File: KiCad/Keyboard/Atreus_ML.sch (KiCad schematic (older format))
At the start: 88 parts, among them K1 CHERRY_ML, K10 CHERRY_ML, K11 CHERRY_ML, K12 CHERRY_ML, K13 CHERRY_ML, K14 CHERRY_ML, K15 CHERRY_ML, K16 CHERRY_ML, K17 CHERRY_ML, K18 CHERRY_ML, K19 CHERRY_ML, K2 CHERRY_ML, K20 CHERRY_ML, K21 CHERRY_ML, K22 CHERRY_ML, K23 CHERRY_ML, K24 CHERRY_ML, K25 CHERRY_ML, K26 CHERRY_ML, K27 CHERRY_ML, K28 CHERRY_ML, K29 CHERRY_ML, K3 CHERRY_ML, K30 CHERRY_ML, K31 CHERRY_ML, K32 CHERRY_ML, K33 CHERRY_ML, K34 CHERRY_ML, K35 CHERRY_ML, K36 CHERRY_ML, K37 CHERRY_ML, K38 CHERRY_ML, K39 CHERRY_ML, K4 CHERRY_ML, K40 CHERRY_ML, K41 CHERRY_ML, K42 CHERRY_ML, K5 CHERRY_ML, K6 CHERRY_ML, K7 CHERRY_ML, K8 CHERRY_ML, K9 CHERRY_ML, P1 CONN_01X07, P2 CONN_01X07, P3 CONN_01X07, U1 TEENSY2.0-Compact

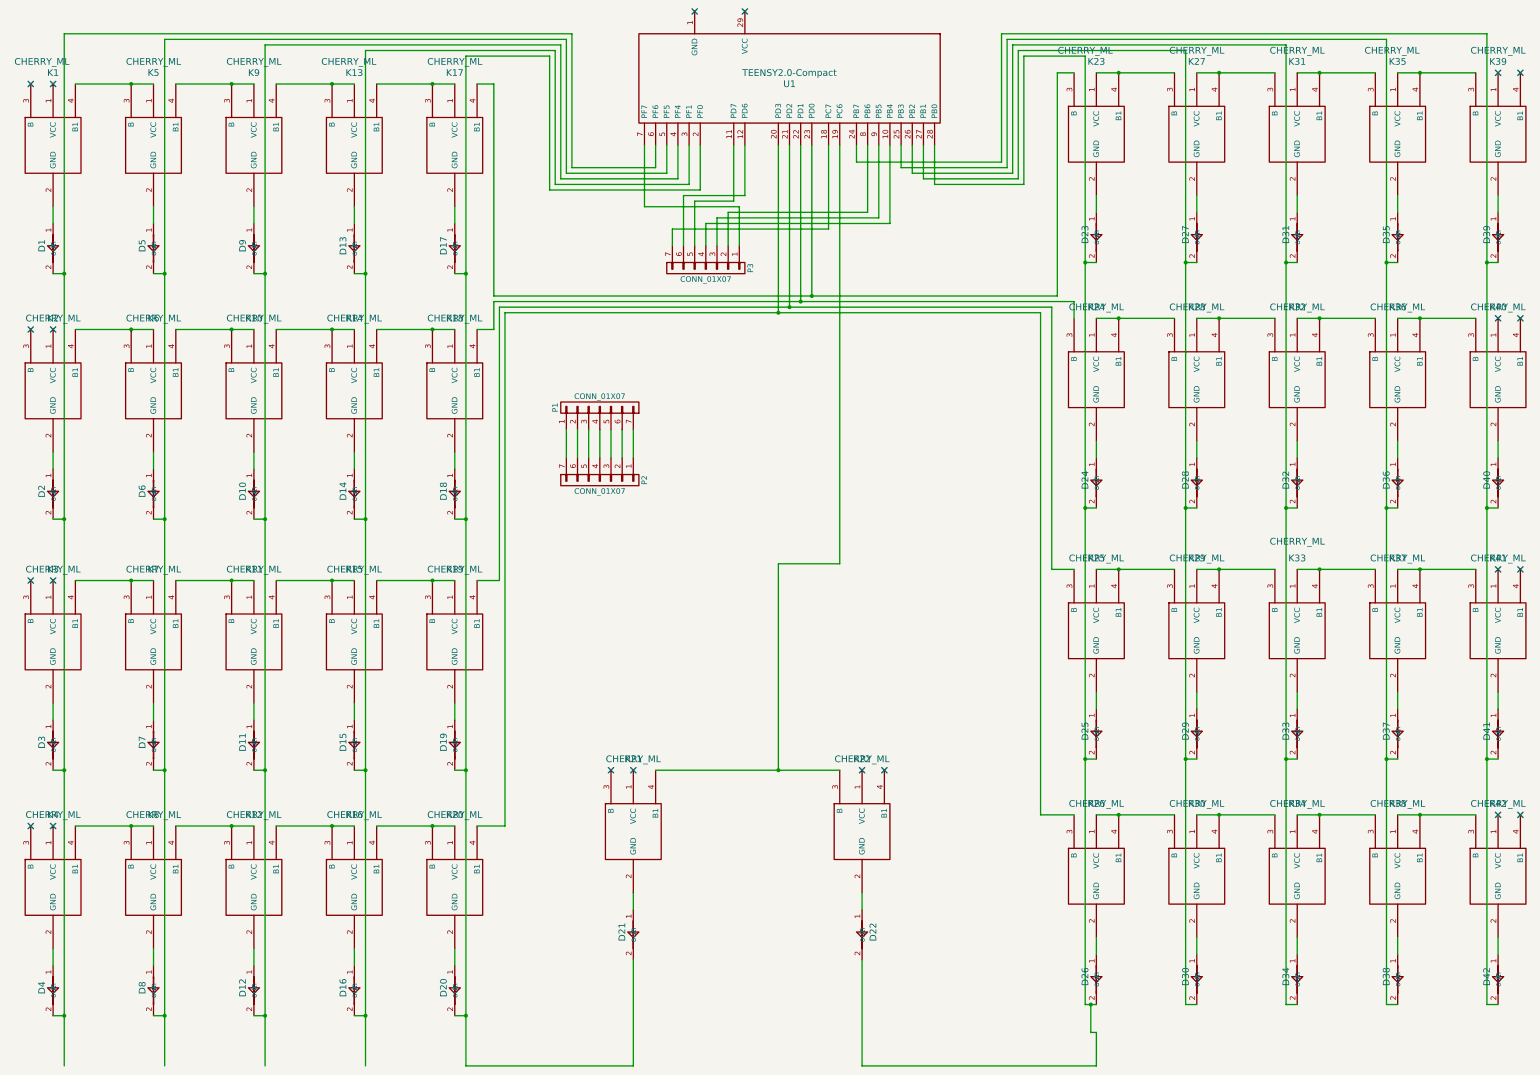
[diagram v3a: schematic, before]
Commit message: Half a fix for design and some test code
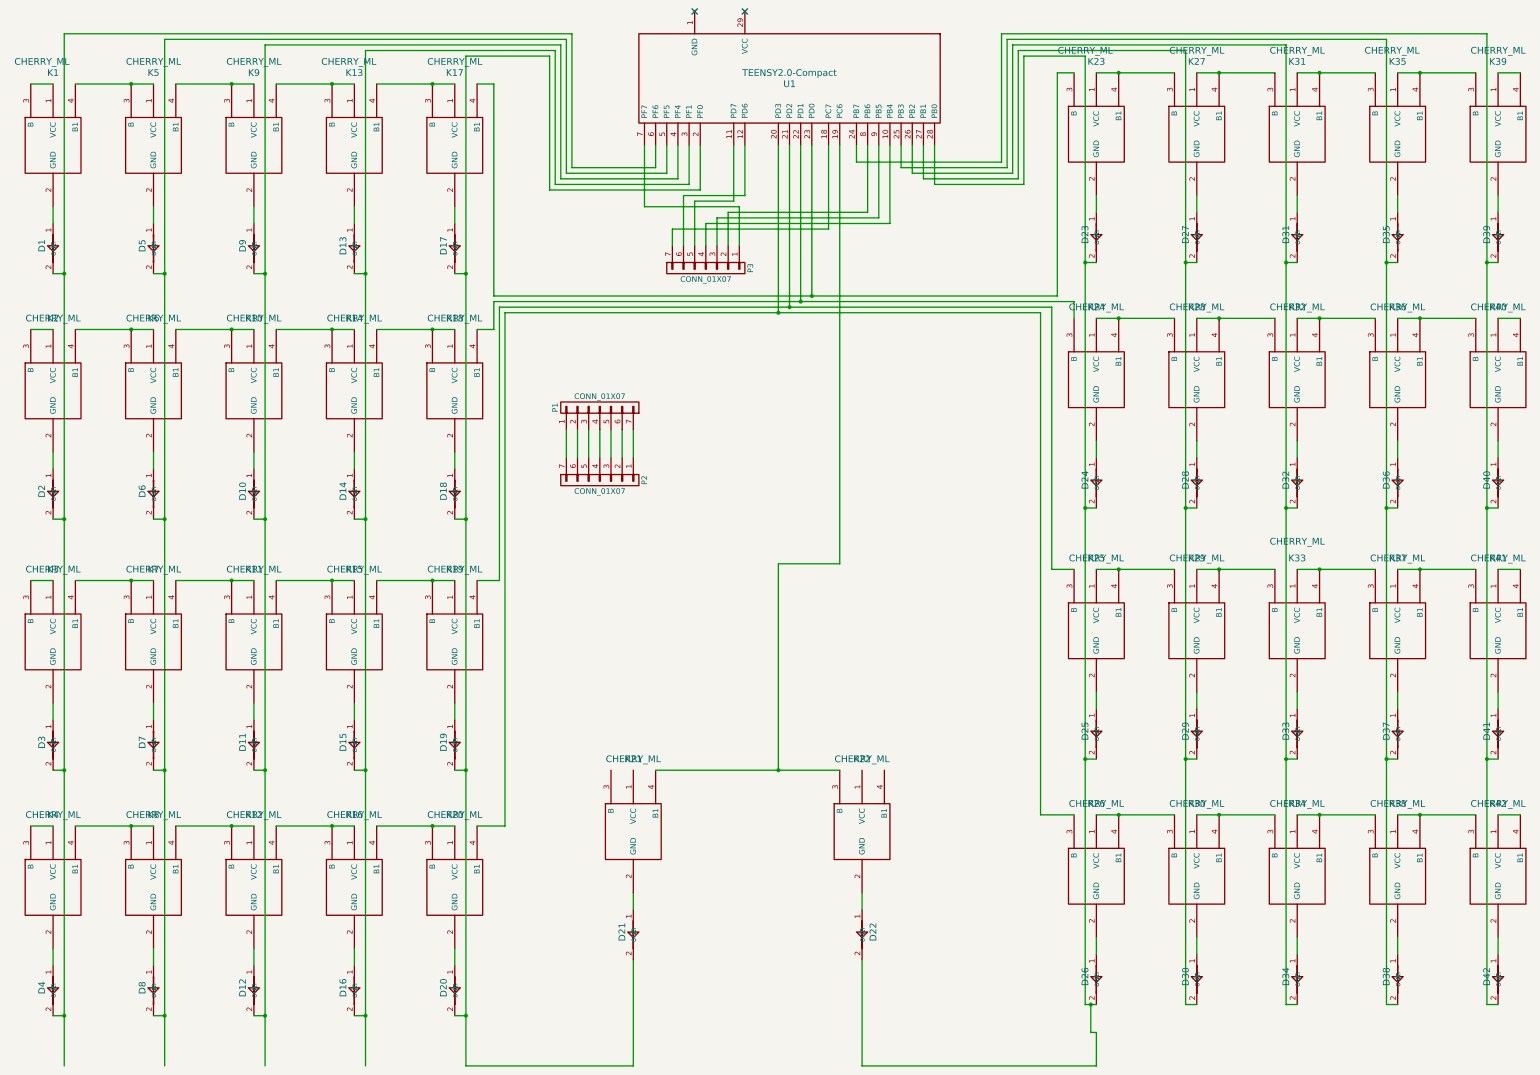
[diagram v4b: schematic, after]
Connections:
- net at K1.1 (VCC): now also K1.3 (B)
- net at K2.1 (VCC): now also K2.3 (B)
- net at K3.1 (VCC): now also K3.3 (B)
- net at K4.1 (VCC): now also K4.3 (B)
- net at K39.1 (VCC): now also K39.4 (B1)
- net at K40.1 (VCC): now also K40.4 (B1)
- net at K41.1 (VCC): now also K41.4 (B1)
- net at K42.1 (VCC): now also K42.4 (B1)
- no-connect marks 22 -> 2
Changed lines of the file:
@@
 LIBS:contrib
 LIBS:valves
-LIBS:4148_rev2
-LIBS:cherry_ml
 LIBS:components
 LIBS:Atreus_ML-cache
-EELAYER 25 0
+EELAYER 27 0
 EELAYER END
 $Descr A3 16535 11693
@@
 Sheet 1 1
 Title ""
-Date "21 mar 2016"
+Date "6 apr 2016"
 Rev ""
 Comp ""
@@
 	0    -1   1    0
 $EndComp
-NoConn ~ 1950 7850
-NoConn ~ 2150 7850
-NoConn ~ 1950 5650
-NoConn ~ 2150 5650
-NoConn ~ 1950 3400
-NoConn ~ 2150 3400
-NoConn ~ 1950 1200
-NoConn ~ 2150 1200
-NoConn ~ 7150 7350
-NoConn ~ 7350 7350
 $Comp
 L CHERRY_ML K23
@@
 	1    0    0    -1
 $EndComp
-NoConn ~ 15300 1100
-NoConn ~ 15100 1100
-NoConn ~ 15100 3300
-NoConn ~ 15300 3300
-NoConn ~ 15300 7750
-NoConn ~ 15100 7750
-NoConn ~ 15300 5550
-NoConn ~ 15100 5550
 $Comp
 L TEENSY2.0-Compact U1
@@
 	1    0    0    -1
 $EndComp
-NoConn ~ 9400 7350
-NoConn ~ 9600 7350
 Wire Wire Line
 	7550 7350 9200 7350
@@
 Wire Wire Line
 	7800 2200 7800 2650
+Wire Wire Line
+	1950 1200 2150 1200
+Wire Wire Line
+	1950 3400 2150 3400
+Wire Wire Line
+	1950 5650 2150 5650
+Wire Wire Line
+	1950 7850 2150 7850
+Wire Wire Line
+	15300 7750 15100 7750
+Wire Wire Line
+	15300 5550 15100 5550
+Wire Wire Line
+	15300 3300 15100 3300
+Wire Wire Line
+	15300 1100 15100 1100
 $EndSCHEMATC

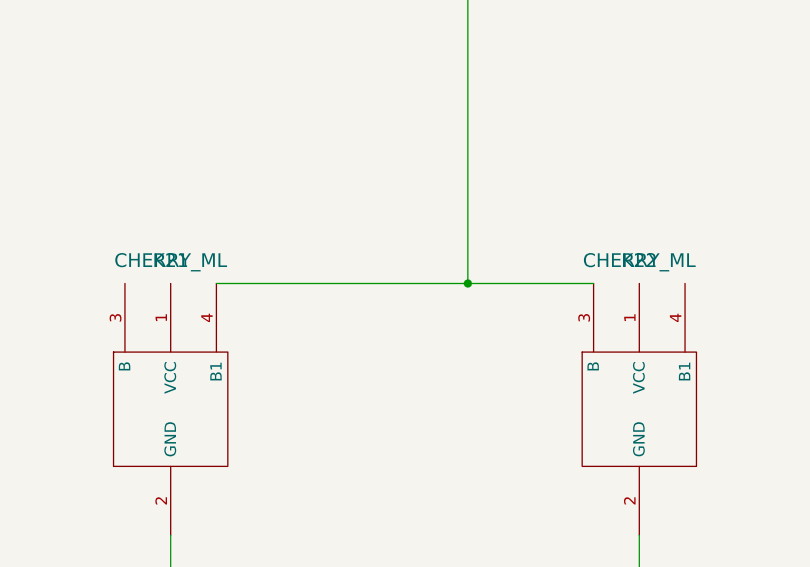
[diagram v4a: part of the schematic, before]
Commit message: Fixing design whoopsie
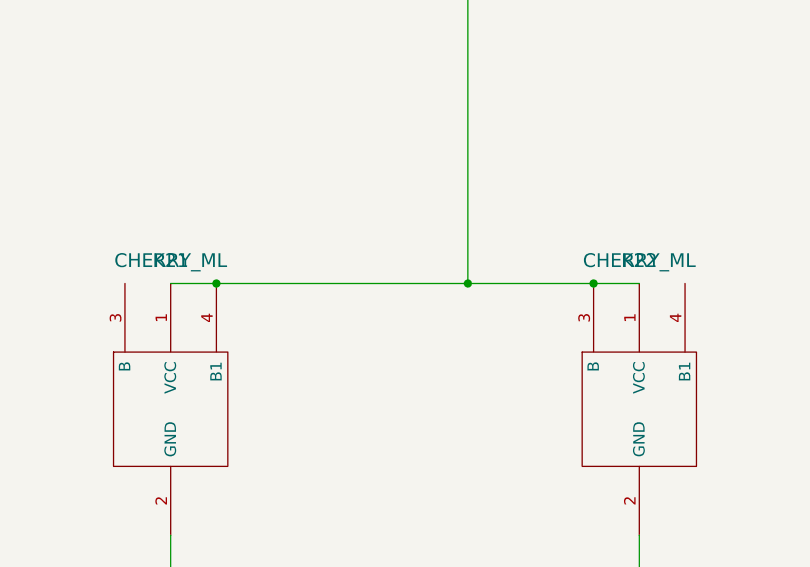
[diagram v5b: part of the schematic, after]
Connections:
- net at K21.1 (VCC): now also K21.4 (B1), K22.1 (VCC), K22.3 (B), U1.19 (PC6)
